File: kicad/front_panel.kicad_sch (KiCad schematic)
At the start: 0 parts

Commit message: Add front panel schematic based on 74HC164
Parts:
- added C112: 100n, Capacitor_SMD:C_0805_2012Metric_Pad1.18x1.45mm_HandSolder, symbol Device:C
- added J27: Conn_01x07_Socket, symbol Connector:Conn_01x07_Socket
- added R108, R109: 22k_0603, Resistor_SMD:R_0805_2012Metric_Pad1.20x1.40mm_HandSolder, symbol PCM_4ms_Resistor:22k_0603
- added R110: 1k, Resistor_SMD:R_0805_2012Metric_Pad1.20x1.40mm_HandSolder, symbol Device:R
- added SW1, SW2, SW3, SW4, SW5, SW6, SW7: SW_Push, symbol Switch:SW_Push
- added U18: ~, symbol custom_symbols:S1D157xx
- added U19: 74HC164, symbol 74xx:74HC164
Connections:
- new net: C112.1, J27.2 (Pin_2), R108.1, U18. (~{WR}), U19.14 (VCC), U19.9 (~{MR})
- new net: J27.3 (Pin_3), R110.2
- new net: J27.4 (Pin_4), U18. (~{WR}), U19.1 (DSA), U19.2 (DSB)
- new net: J27.5 (Pin_5), U18. (~{WR})
- new net: J27.6 (Pin_6), U18. (~{WR})
- new net: J27.7 (Pin_7), R109.2, U19.8 (CP)
- new net: R108.2, R110.1, SW1.2, SW2.1, SW3.2, SW4.2, SW5.1, SW6.1, SW7.1
- new net: SW3.1, U18. (~{WR}), U19.3 (Q0)
- new net: SW5.2, U18. (~{WR}), U19.10 (Q4)
- new net: SW7.2, U18. (~{WR}), U19.12 (Q6)
- new net: SW6.2, U18. (~{WR}), U19.11 (Q5)
- new net: U18. (~{WR}), U19.13 (Q7)
- new net: SW4.1, U18. (~{WR}), U19.4 (Q1)
- new net: SW1.1, U18. (~{WR}), U19.5 (Q2)
- new net: SW2.2, U18. (~{WR}), U19.6 (Q3)
- new net GND: C112.2, J27.1 (Pin_1), R109.1, U18. (~{WR}), U19.7 (GND)
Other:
- note added: "Context1"
- note added: "Context2"
- note added: "Context3"
- note added: "Iron1"
- note added: "Iron2"
- note added: "Iron3"
- note added: "Mode/Menu"

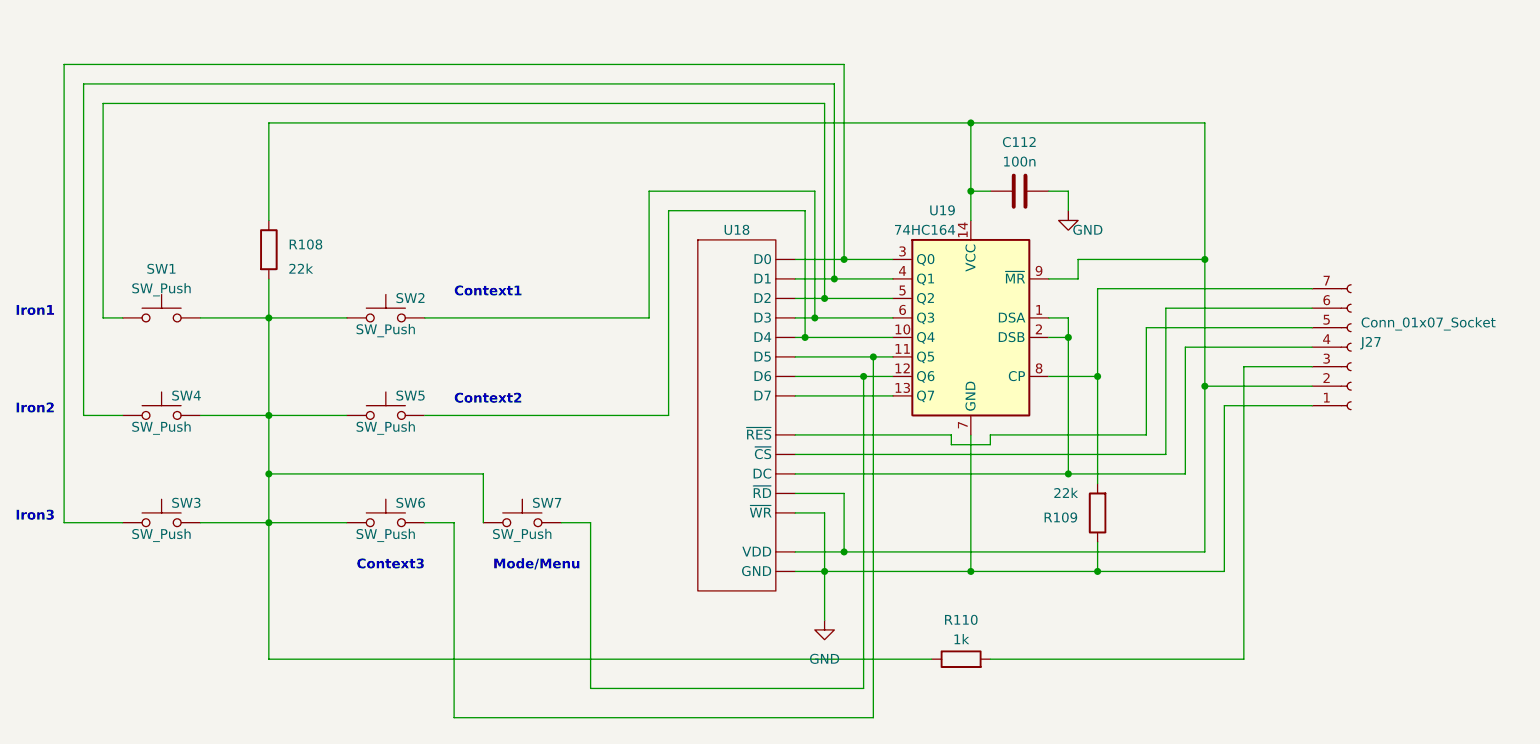
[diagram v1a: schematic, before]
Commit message: Fix front panel sch
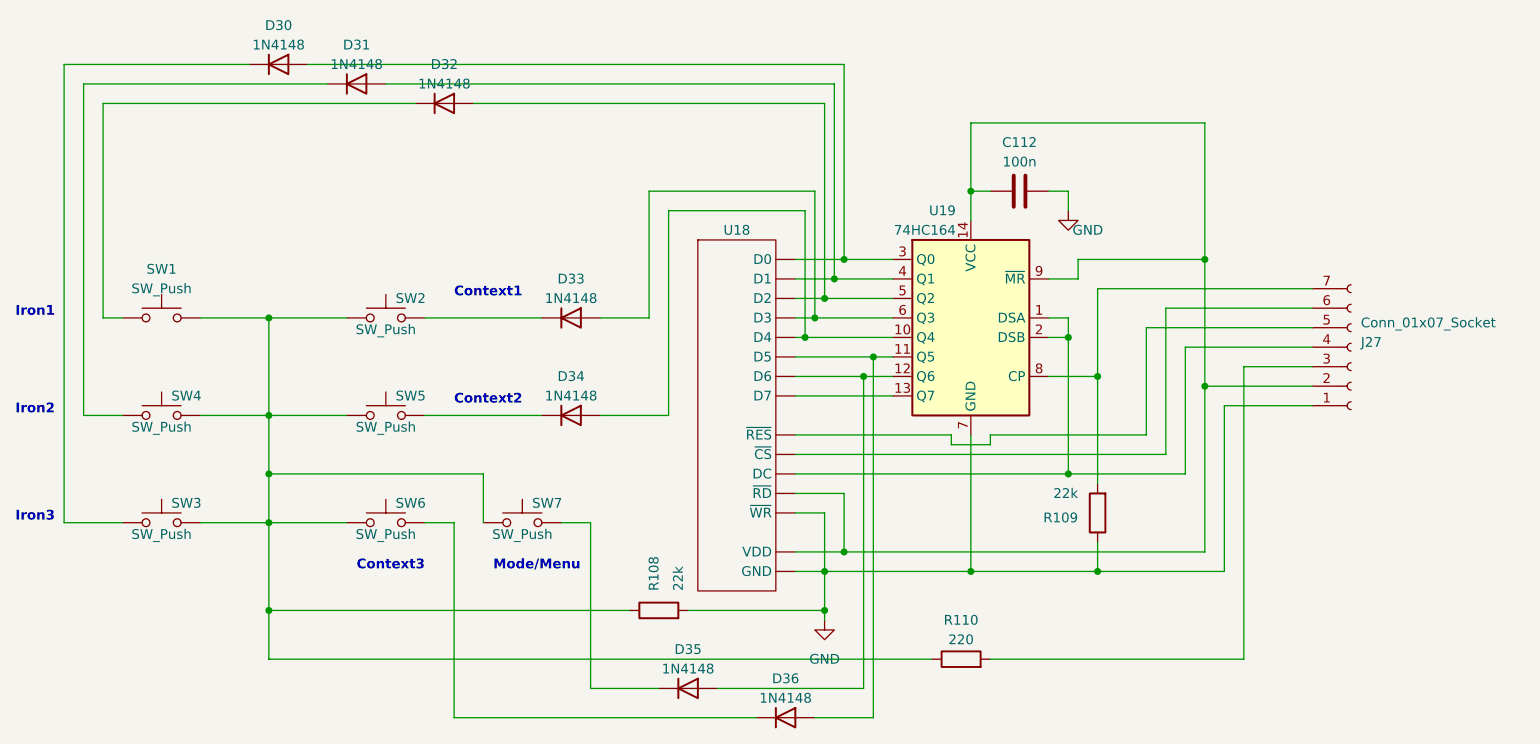
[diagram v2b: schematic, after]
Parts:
- added D30, D31, D32, D33, D34, D35, D36: 1N4148, Diode_THT:D_DO-35_SOD27_P7.62mm_Horizontal, symbol Diode:1N4148
- R110: value 1k -> 220
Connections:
- net GND: now also R108.2
- net at C112.1, J27.2 (Pin_2), U18. (~{WR})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: no longer R108.1
- net at R110.1, SW1.2, SW2.1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: now also R108.1; no longer R108.2
- new net: D30.1 (K), SW3.1
- new net: D34.1 (K), SW5.2
- new net: D35.1 (K), SW7.2
- new net: D34.2 (A), U18. (~{WR}), U19.10 (Q4)
- new net: D36.2 (A), U18. (~{WR}), U19.11 (Q5)
- new net: D35.2 (A), U18. (~{WR}), U19.12 (Q6)
- new net: D30.2 (A), U18. (~{WR}), U19.3 (Q0)
- new net: D31.2 (A), U18. (~{WR}), U19.4 (Q1)
- new net: D32.2 (A), U18. (~{WR}), U19.5 (Q2)
- new net: D33.2 (A), U18. (~{WR}), U19.6 (Q3)
- new net: D31.1 (K), SW4.1
- new net: D36.1 (K), SW6.2
- new net: D33.1 (K), SW2.2
- new net: D32.1 (K), SW1.1
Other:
- moved on the sheet: R108

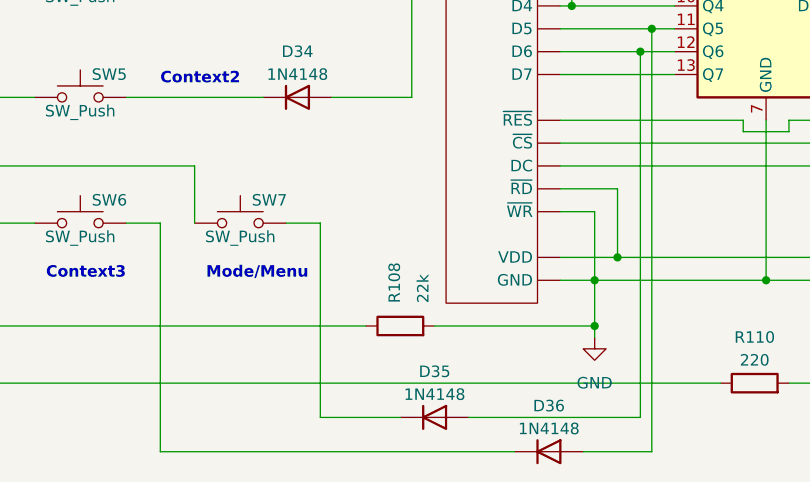
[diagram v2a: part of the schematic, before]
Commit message: Implement keyboard polling
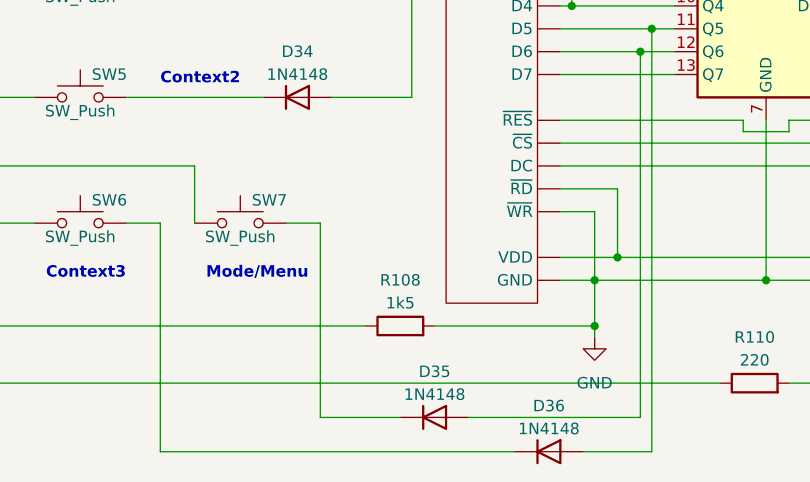
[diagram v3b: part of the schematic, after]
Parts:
- removed R108: 22k_0603, Resistor_SMD:R_0805_2012Metric_Pad1.20x1.40mm_HandSolder, symbol PCM_4ms_Resistor:22k_0603
- added R108: 1k5, symbol Device:R
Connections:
- net GND: now also R108.2
- net at R110.1, SW1.2, SW2.1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: now also R108.1
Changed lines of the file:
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@@
     )
   )
-  (symbol (lib_id "PCM_4ms_Resistor:22k_0603") (at 109.22 110.49 90) (unit 1)
-    (in_bom yes) (on_board yes) (dnp no)
-    (property "Reference" "R108" (at 108.585 107.95 0)
-      (effects (font (size 1.27 1.27)) (justify left))
+  (symbol (lib_id "Device:R") (at 109.22 110.49 90) (unit 1)
+    (in_bom yes) (on_board yes) (dnp no) (fields_autoplaced)
+    (property "Reference" "R108" (at 109.22 105.41 90)
+      (effects (font (size 1.27 1.27)))
     )
-    (property "Value" "22k_0603" (at 109.22 113.03 90)
+    (property "Value" "1k5" (at 109.22 107.95 90)
+      (effects (font (size 1.27 1.27)))
+    )
+    (property "Footprint" "" (at 109.22 112.268 90)
       (effects (font (size 1.27 1.27)) hide)
     )
-    (property "Footprint" "Resistor_SMD:R_0805_2012Metric_Pad1.20x1.40mm_HandSolder" (at 121.92 113.03 0)
-      (effects (font (size 1.27 1.27)) (justify left) hide)
-    )
-    (property "Datasheet" "" (at 109.22 110.49 0)
+    (property "Datasheet" "~" (at 109.22 110.49 0)
       (effects (font (size 1.27 1.27)) hide)
     )
-    (property "Specifications" "22K, 1%, 1/10W, 0603" (at 117.094 113.03 0)
-      (effects (font (size 1.27 1.27)) (justify left) hide)
-    )
-    (property "Manufacturer" "Yageo" (at 118.618 113.03 0)
-      (effects (font (size 1.27 1.27)) (justify left) hide)
-    )
-    (property "Part Number" "RC0603FR-0722KL" (at 120.142 113.03 0)
-      (effects (font (size 1.27 1.27)) (justify left) hide)
-    )
-    (property "Display" "22k" (at 111.76 107.95 0)
-      (effects (font (size 1.27 1.27)) (justify left))
-    )
-    (property "JLCPCB ID" "C31850" (at 109.22 106.68 90)
-      (effects (font (size 1.27 1.27)) hide)
-    )
